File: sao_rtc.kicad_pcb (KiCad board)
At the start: 2 copper layers, 19.6 x 24.7 mm, 8 parts, among them J1 Conn_02x03_Odd_Even, U1 PCF8563DRG, Y1 Crystal

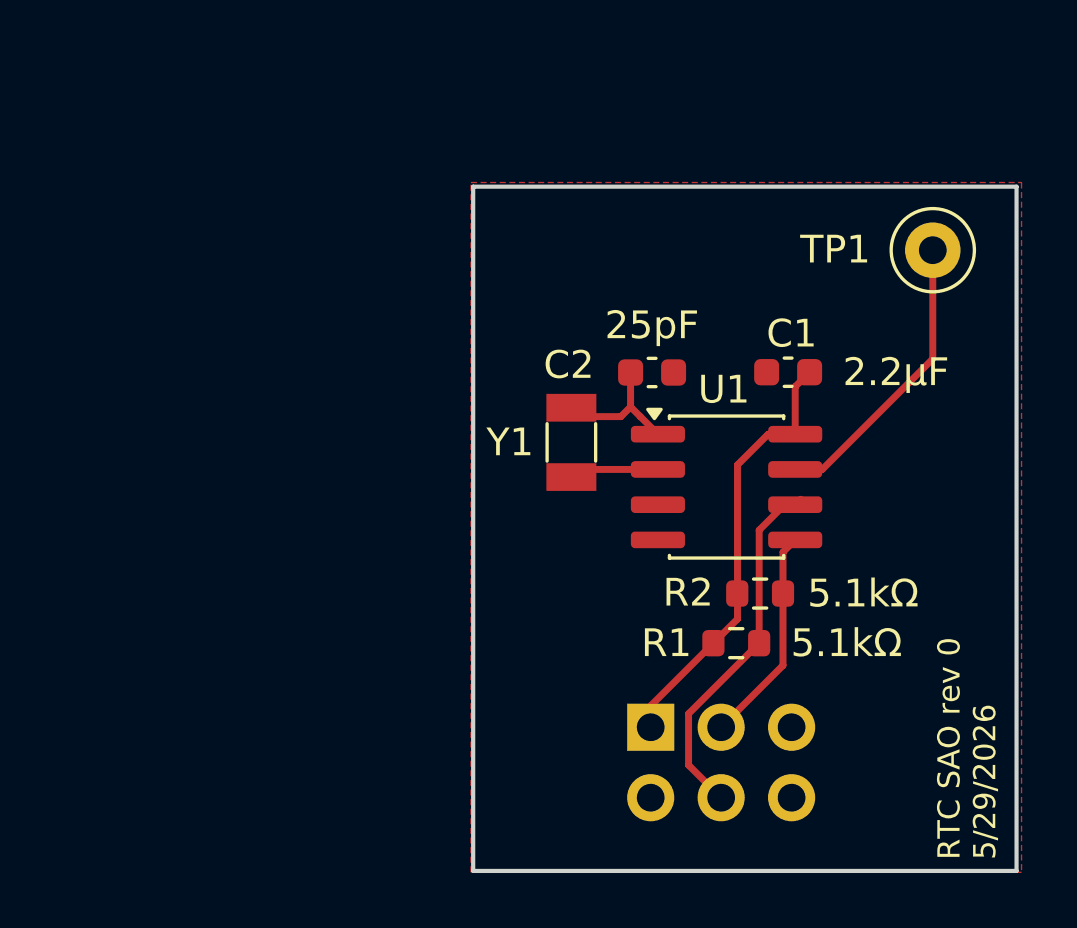
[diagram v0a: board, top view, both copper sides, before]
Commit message: scope creep is a hell of a drug
Add AW320001 BMS and associated stuff
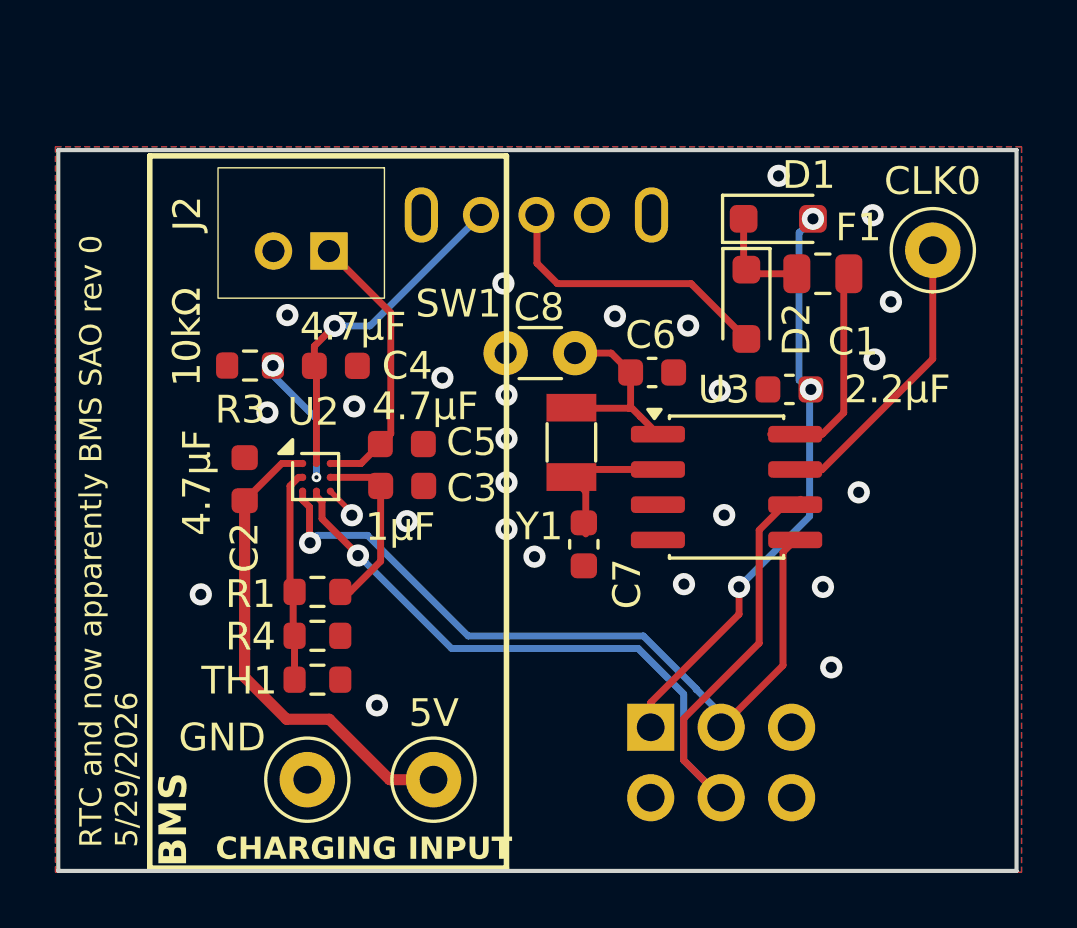
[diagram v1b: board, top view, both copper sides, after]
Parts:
- removed R2: 5.1kΩ, Resistor_SMD:R_0603_1608Metric
- added 5VIN1: 5V, TestPoint:TestPoint_Loop_D2.50mm_Drill1.0mm, F.Cu at (94.3, 83.5)
- added C2: 4.7μF, sao:C_0603_1608Metric, F.Cu at (87.5, 72.6)
- added C3: 1μF, sao:C_0603_1608Metric, F.Cu at (93.2, 72.9)
- added C4: 4.7μF, sao:C_0603_1608Metric, F.Cu at (90.8, 68.5)
- added C5: 4.7μF, sao:C_0603_1608Metric, F.Cu at (93.2, 71.4)
- added C7: ~, Capacitor_SMD:C_0603_1608Metric, F.Cu at (99.8, 75.0)
- added C8: C, Capacitor_THT:C_Disc_D3.0mm_W1.6mm_P2.50mm, F.Cu at (99.4, 68.1)
- added D1: D_Zener, Diode_SMD:D_SOD-323_HandSoldering, F.Cu at (106.8, 63.2)
- added D2: D_Zener, Diode_SMD:D_SOD-323_HandSoldering, F.Cu at (105.6, 66.3)
- added F1: Polyfuse, Fuse:Fuse_0805_2012Metric, F.Cu at (108.4, 65.2)
- added GND1: GND, TestPoint:TestPoint_Loop_D2.50mm_Drill1.0mm, F.Cu at (89.8, 83.5)
- added J2: S2B-PH-K-S(LF)(SN), Connector_PinHeader_2.00mm:PinHeader_1x02_P2.00mm_Horizontal, F.Cu at (90.6, 64.4)
- added R3: 10kΩ, Resistor_SMD:R_0603_1608Metric, F.Cu at (87.7, 68.5)
- added R4: Ω, Resistor_SMD:R_0603_1608Metric, F.Cu at (90.1, 78.3)
- added SW1: SW_SPDT_1825232-1, Swadge_Parts:1825232-1, F.Cu at (98.0, 63.1)
- added TH1: Thermistor_NTC, Resistor_SMD:R_0603_1608Metric, F.Cu at (90.1, 79.9)
- added U2: AW32001ECSR, Package_CSP:WLCSP-9_1.21x1.22mm_Layout3x3_P0.4mm, F.Cu at (90.0, 72.5)
- R1: value 5.1kΩ -> Ω
- moved R1 15.2 mm to (90.1, 76.7), turned to 0 degrees
- moved C1 0.62 mm to (107.2, 69.4)
- renumbered C2 to C6, TP1 to CLK0, U1 to U3
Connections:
- R1 pad 1: SCL -> Net-(U2-NTC)
- R1 pad 2: 3V3 -> AW32_VDD
- U3 pad 8: 3V3 -> Net-(U3-VDD)
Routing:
- net SCL: track 13.1 -> 34.3 mm, vias 0 -> 1
- net SDA: track 7.97 -> 28.0 mm, vias 0 -> 1
- net +5V: track 0.00 -> 17.4 mm
- net VOUT: track 0.00 -> 12.2 mm, vias 0 -> 1
- net Net-(D2-A): track 0.00 -> 10.4 mm
- net BATT+: track 0.00 -> 10.1 mm
- net Net-(U3-VDD): track 0.00 -> 8.09 mm
- net Net-(U2-NTC): track 0.00 -> 7.64 mm
- net AW32_VDD: track 0.00 -> 6.62 mm
- net 3V3: track 15.8 -> 21.2 mm, vias 0 -> 3
- net Net-(U2-INT): track 0.00 -> 4.68 mm, vias 0 -> 2
- net Net-(D1-K): track 0.00 -> 3.75 mm
- net Net-(U3-OSCI): track 4.88 -> 7.28 mm
- net Net-(U3-OSCO): track 3.34 -> 5.60 mm
- net GND: track 0.00 -> 1.19 mm, vias 0 -> 26
- added copper zone on B.Cu, net GND
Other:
- board size 19.6 x 24.7 mm -> 34.5 x 26 mm
- board text added: "BMS"
- board text added: "CHARGING INPUT"
- board text added: "RTC and now apparently BMS SAO rev 0 5/29/2026"
- board text removed: "RTC SAO rev 0 5/29/2026"

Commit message: update schematic for voltage regulation
she creeped my scope until I swadged her
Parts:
- added C10: 1μF, Capacitor_SMD:C_0603_1608Metric, F.Cu at (54.8, 72.8)
- added C11: 120 pF, Capacitor_SMD:C_0603_1608Metric, F.Cu at (54.8, 75.3)
- added C9: 1μF, Capacitor_SMD:C_0603_1608Metric, F.Cu at (54.8, 70.2)
- added D1: SP0502BAJT, Package_TO_SOT_SMD:SOT-23, F.Cu at (63.4, 81.9)
- added D2: 4.3V, Diode_SMD:D_SOD-323_HandSoldering, F.Cu at (55.3, 83.0)
- added D3: D, Diode_SMD:D_SMA, F.Cu at (64.8, 75.9)
- added F1: 500mA PTC, Fuse:Fuse_0805_2012Metric, F.Cu at (67.9, 83.4)
- added L1: 2.2uH, Inductor_SMD:L_1008_2520Metric, F.Cu at (68.2, 80.1)
- added R10: 43kΩ, Resistor_SMD:R_0603_1608Metric, F.Cu at (58.8, 80.3)
- added R2: Ω, Resistor_SMD:R_0603_1608Metric, F.Cu at (54.8, 77.8)
- added R4: 10kΩ, Resistor_SMD:R_0603_1608Metric, F.Cu at (54.8, 80.3)
- added R6: 10kΩ, Resistor_SMD:R_0603_1608Metric, F.Cu at (58.8, 70.2)
- added R7: 43kΩ, Resistor_SMD:R_0603_1608Metric, F.Cu at (58.8, 72.8)
- added R8: 10kΩ, Resistor_SMD:R_0603_1608Metric, F.Cu at (58.8, 75.3)
- added R9: 43kΩ, Resistor_SMD:R_0603_1608Metric, F.Cu at (58.8, 77.8)
- added U3: M3410, Package_TO_SOT_SMD:SOT-23-5, F.Cu at (68.0, 71.4)
- added VMON1: TestPoint, TestPoint:TestPoint_Loop_D2.50mm_Drill1.0mm, F.Cu at (63.1, 71.3)
- Y1: value Crystal -> 32.768 kHz
- renumbered C8 to C5, C5 to C8, J2 to J1, J1 to J2, R4 to R5, U2 to U1, U3 to U2
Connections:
- C1 pad 1: 3V3 -> Net-(SW1-B)
- C4 pad 1: VOUT -> Net-(D2-A)
- R5 pad 2: Net-(U2-NTC) -> Net-(U1-NTC)
- SW1 pad 1: unconnected-(SW1-A-Pad1) -> 3V3
- SW1 pad 2: Net-(D2-A) -> Net-(SW1-B)
- SW1 pad 3: VOUT -> 3V3 SAO
- TH1 pad 1: Net-(U2-NTC) -> Net-(U1-NTC)
- U1 pad A2: VOUT -> Net-(D2-A)
- U1 pad B1: Net-(U2-NTC) -> Net-(U1-NTC)
- U1 pad B2: Net-(U2-INT) -> Net-(U1-INT)
- U2 pad 8: Net-(U3-VDD) -> Net-(SW1-B)
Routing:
- net VOUT: track 12.2 -> 0.00 mm, vias 1 -> 0
- net Net-(D2-A): track 10.4 -> 22.7 mm, vias 0 -> 1
- net Net-(U2-INT): vias 2 -> 1
- net Net-(U1-INT): vias 0 -> 1

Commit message: routed and ordered
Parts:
- removed 5VIN1: 5V, TestPoint:TestPoint_Loop_D2.50mm_Drill1.0mm
- removed the D1 at (106.8, 63.2)
- removed the D2 at (105.6, 66.3)
- removed the F1 at (108.4, 65.2)
- removed GND1: GND, TestPoint:TestPoint_Loop_D2.50mm_Drill1.0mm
- removed R1: Ω, Resistor_SMD:R_0603_1608Metric
- removed R3: 10kΩ, Resistor_SMD:R_0603_1608Metric
- added D4: 3V3 ON, LED_SMD:LED_0603_1608Metric, F.Cu at (119.2, 81.8)
- added D5: RTC ON, LED_SMD:LED_0603_1608Metric, F.Cu at (123.5, 72.5)
- added J3: Conn_02x03_Odd_Even, Connector_PinHeader_2.54mm:PinHeader_2x03_P2.54mm_Vertical, F.Cu at (1.79, 1.79)
- added J3: Conn_02x03_Odd_Even, Swadge_Parts:PinSocket_2x03_P2.54mm_Vertical, F.Cu at (99.0, 88.3)
- added P1: USB_C_Plug_USB2.0, Connector_USB:USB_C_Receptacle_HRO_TYPE-C-31-M-12, F.Cu at (100.0, 63.5)
- added R11: 22Ω, Resistor_SMD:R_0603_1608Metric, F.Cu at (119.9, 79.4)
- added R12: 22Ω, Resistor_SMD:R_0603_1608Metric, F.Cu at (123.5, 74.1)
- SW1: value SW_SPDT_1825232-1 -> DPDT; footprint Swadge_Parts:1825232-1 -> Button_Switch_SMD:SW_DPDT_CK_JS202011JCQN
- moved C11 65.5 mm to (119.0, 88.0), turned to -90 degrees
- moved R10 59.7 mm to (118.2, 85.6)
- moved C9 58.3 mm to (112.0, 81.3)
- moved R6 57.2 mm to (114.4, 83.7), turned to -90 degrees
- moved R8 56.4 mm to (114.0, 87.0), turned to 180 degrees
- moved C10 54.8 mm to (107.7, 87.0), turned to 180 degrees
- moved R7 54.2 mm to (112.0, 83.0), turned to 180 degrees
- moved VMON1 52.9 mm to (115.5, 78.6)
- moved R9 52.9 mm to (110.8, 87.0), turned to 180 degrees
- moved D2 46.6 mm to (101.4, 76.5), turned to 180 degrees
- moved U3 41.2 mm to (108.3, 80.2)
- moved L1 39.6 mm to (107.5, 84.1), turned to 90 degrees
- moved R4 38.0 mm to (92.4, 75.2)
- moved D3 36.3 mm to (101.0, 72.1)
- moved F1 36.0 mm to (103.6, 78.7), turned to 180 degrees
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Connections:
- net Net-(SW1-B) renamed VDD
- J2 pad 5: unconnected-(J2-GPIO1-Pad5) -> Net-(J2-GPIO1)
- J2 pad 6: unconnected-(J2-GPIO2-Pad6) -> Net-(J2-GPIO2)
- SW1 pad 4: GND -> unconnected-(SW1-C-Pad4)
- SW1 pad 5: GND -> 3V3
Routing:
- net SCL: track 34.3 -> 71.0 mm, vias 1 -> 4
- net SDA: track 28.0 -> 59.9 mm, vias 1 -> 3
- net VDD: track 0.00 -> 23.9 mm, vias 0 -> 3
- net 3V3: track 21.2 -> 40.6 mm, vias 3 -> 0
- net Net-(J2-GPIO1): track 0.00 -> 12.6 mm, vias 0 -> 1
- net Net-(J2-GPIO2): track 0.00 -> 12.4 mm
- net Net-(C10-Pad1): track 0.00 -> 11.7 mm
- net Net-(D3-A): track 0.00 -> 11.2 mm
- net Net-(U3-FB): track 0.00 -> 11.2 mm, vias 0 -> 2
- net Net-(U1-NTC): track 0.00 -> 10.2 mm
- net SNODE: track 0.00 -> 9.63 mm
- net Net-(D2-A): track 22.7 -> 13.3 mm, vias 1 -> 2
- net 3V3 SAO: track 0.00 -> 9.27 mm
- net GND: track 1.19 -> 9.49 mm, vias 26 -> 54
- net Net-(U3-VDD): track 8.09 -> 0.00 mm
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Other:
- board size 34.5 x 26 mm -> 44.9 x 32.9 mm
- board text added: "If using Lithium battery, please turn swadge OFF or remove AAs This board can power the swadge"
- board text added: "RTC"
- board text added: "RTC and BMS SAO rev 0 6/3/2026"
- board text added: "Up -> Power from Battery Down -> Power from Swadge"
- board text removed: "CHARGING INPUT"
- board text removed: "RTC and now apparently BMS SAO rev 0 5/29/2026"

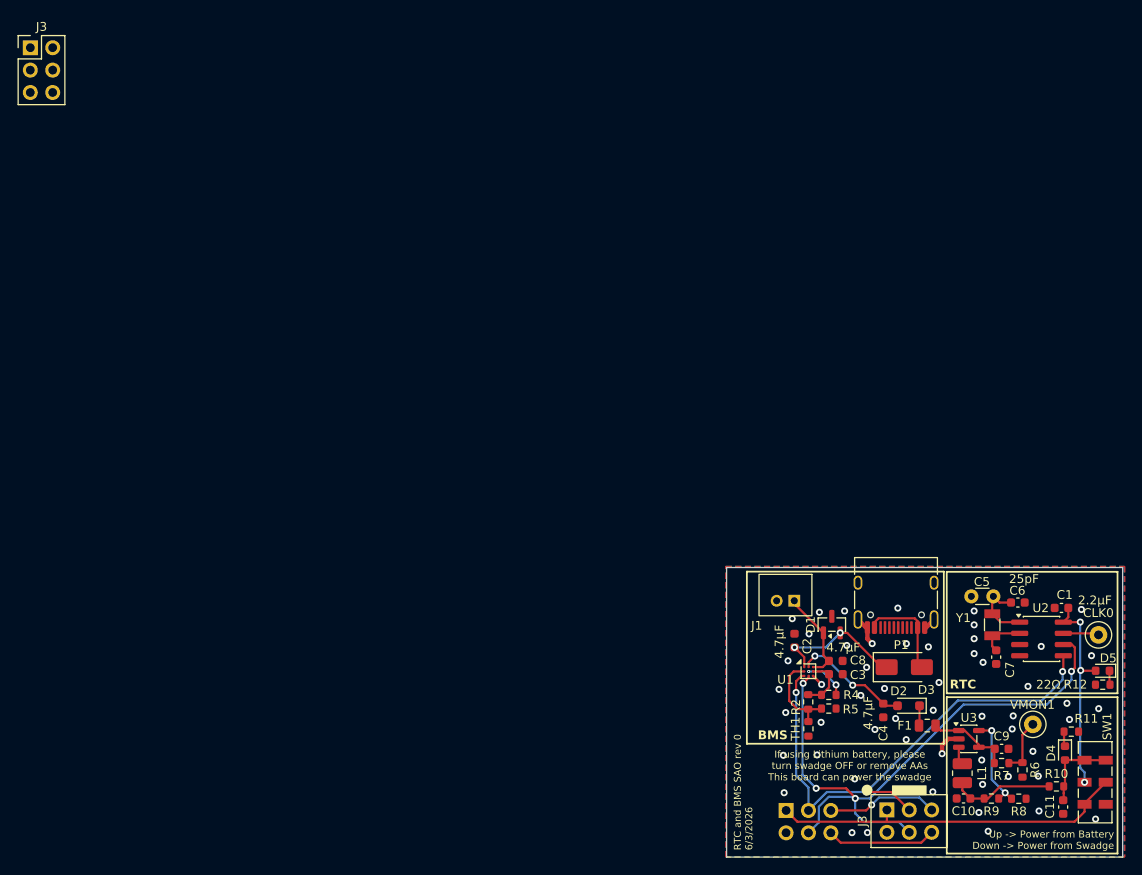
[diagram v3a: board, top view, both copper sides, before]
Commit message: adjust low pass filter
change LC values for part sourcing
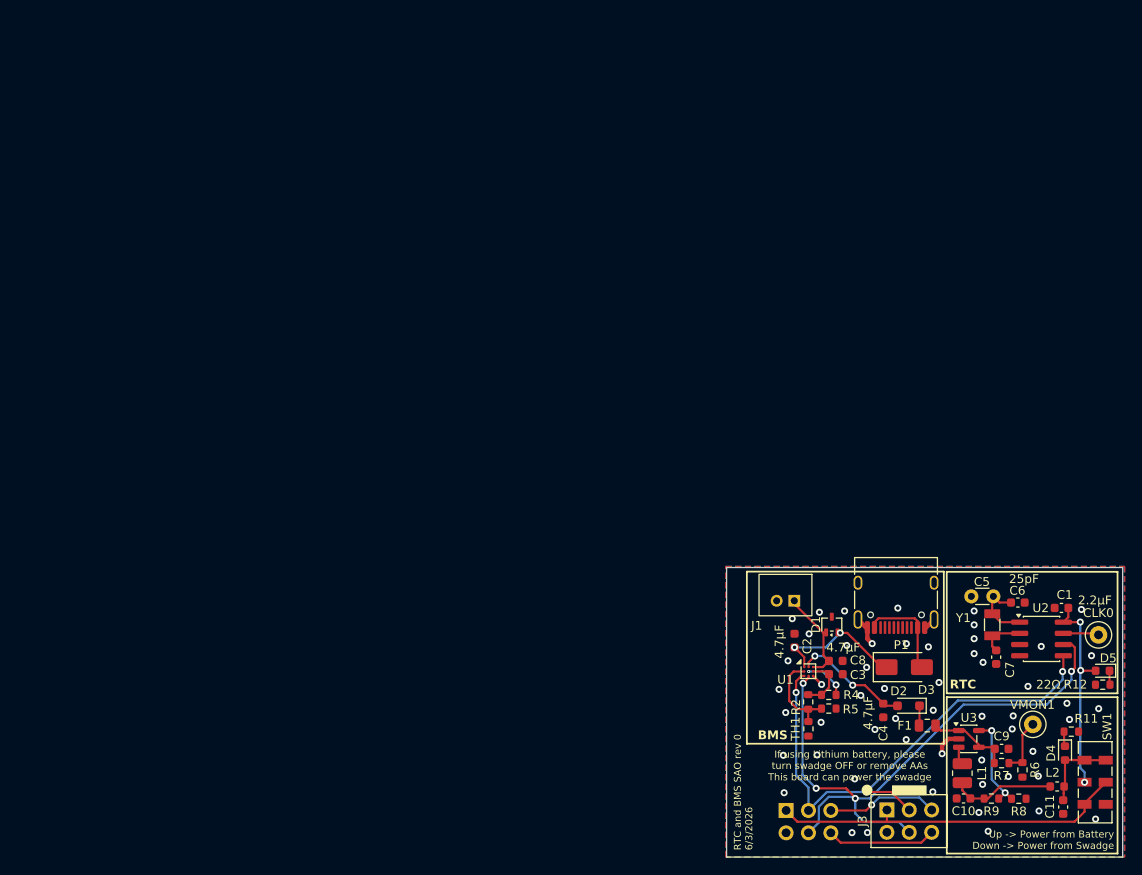
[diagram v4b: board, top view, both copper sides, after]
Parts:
- removed the J3 at (1.79, 1.79)
- removed R10: 43kΩ, Resistor_SMD:R_0603_1608Metric
- added L2: 2.2uH, Inductor_SMD:L_0603_1608Metric, F.Cu at (118.3, 85.6)
- C11: value 120 pF -> 12uF
- D1: footprint Package_TO_SOT_SMD:SOT-23 -> Package_TO_SOT_SMD:SOT-323_SC-70
